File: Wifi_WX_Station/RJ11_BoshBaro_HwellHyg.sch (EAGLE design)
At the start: 8 parts, among them U1 HIH_6130

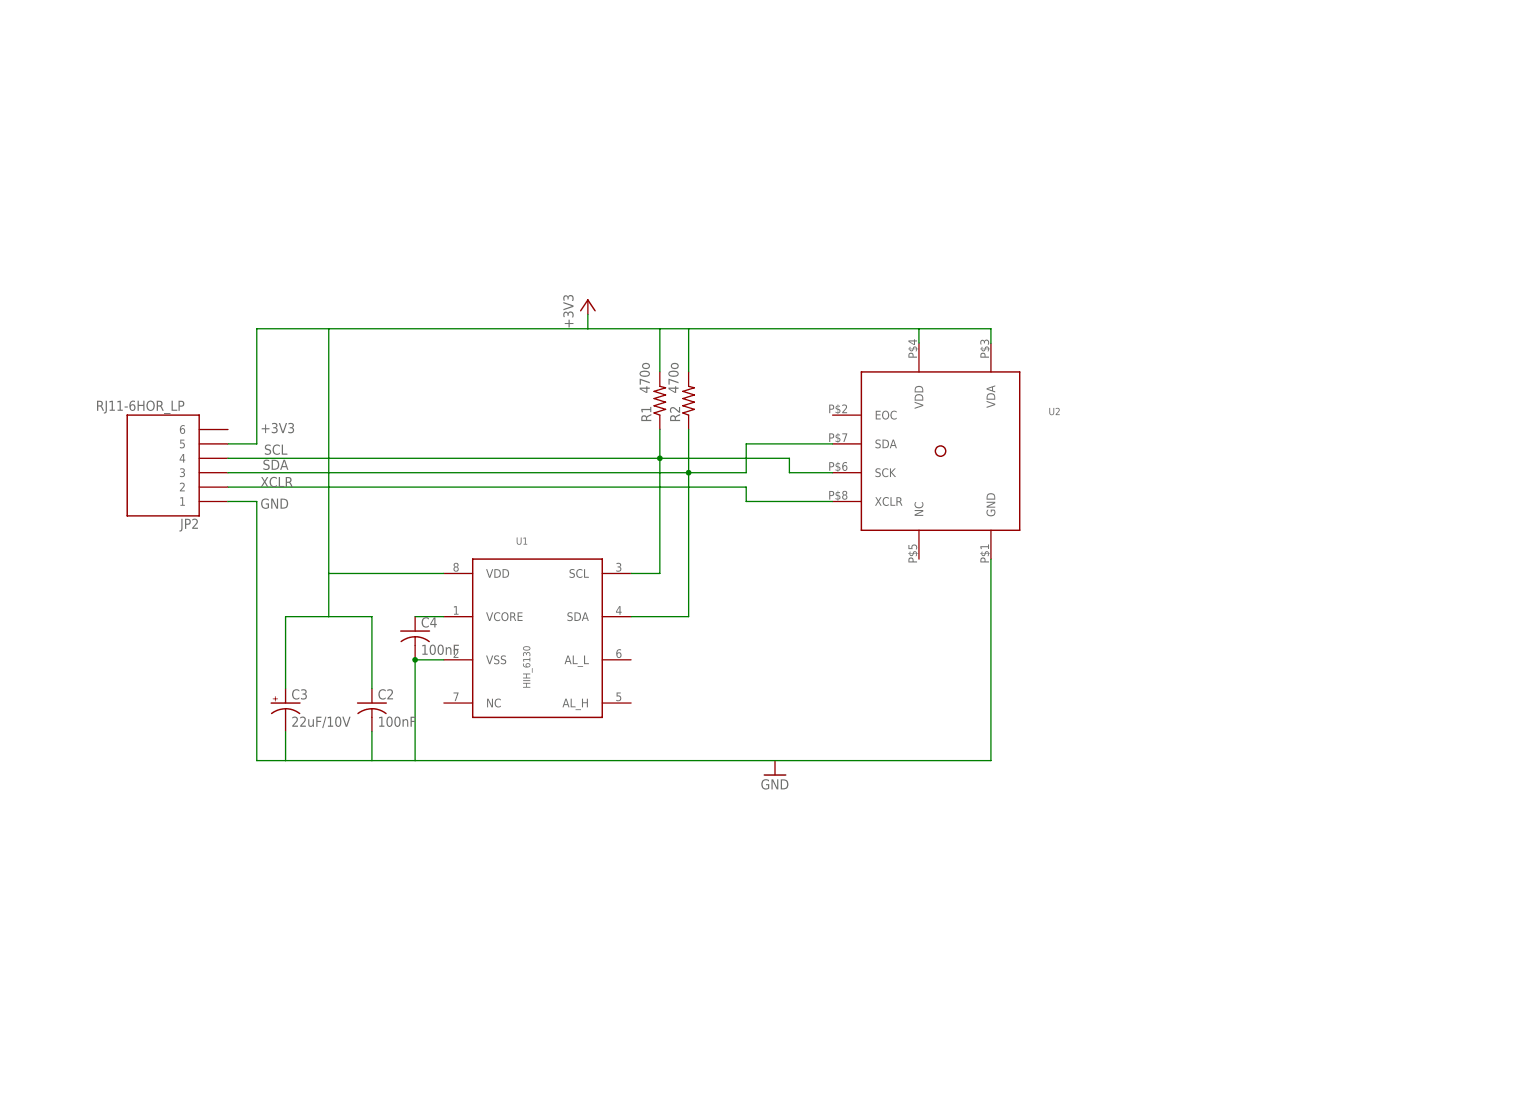
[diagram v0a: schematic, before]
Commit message: added SILabs Hygrometer board Added frames to the schematics
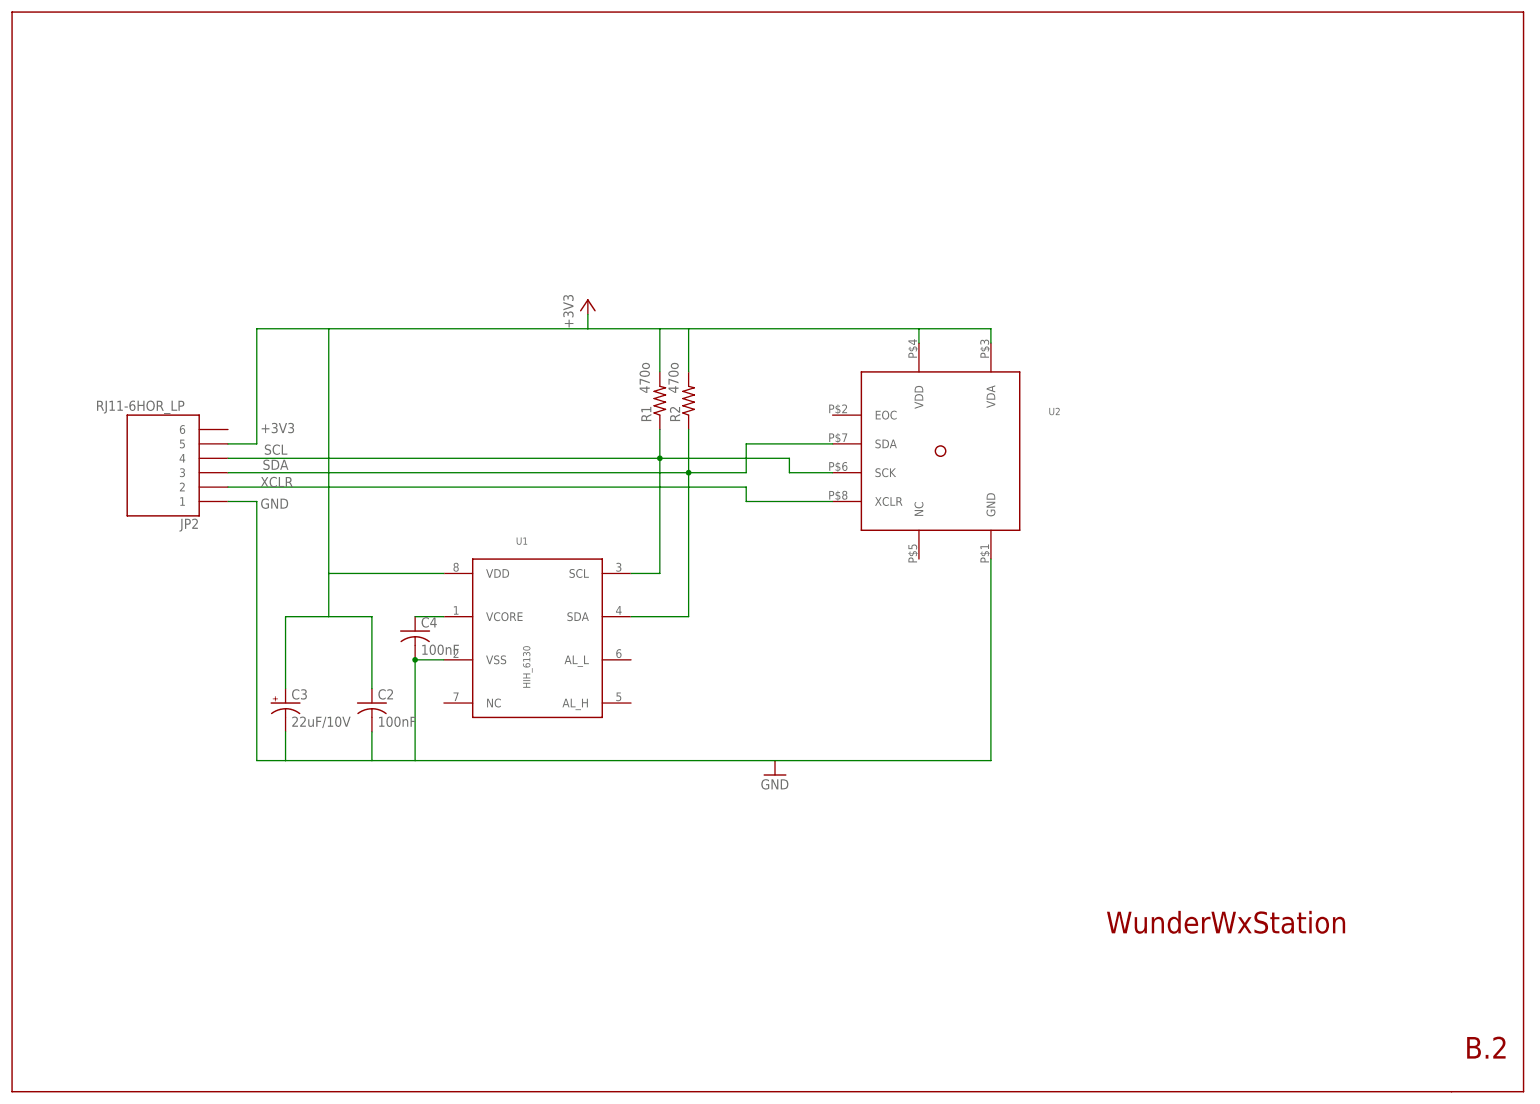
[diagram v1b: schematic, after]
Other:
- note added: "B.2"
- note added: "WunderWxStation"
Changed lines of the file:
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@@
 <part name="U2" library="1AA_Stofer" deviceset="BMP085" device=""/>
 <part name="JP2" library="wifi_WX" deviceset="RJ11-6" device="HOR_LP"/>
+<part name="U$1" library="1AA_Stofer" deviceset="8.5X11" device=""/>
 </parts>
 <sheets>
 <sheet>
 <plain>
+<text x="157.48" y="-30.48" size="3.81" layer="94" ratio="20">WunderWxStation</text>
+<text x="220.726" y="-52.578" size="3.81" layer="94" ratio="20">B.2</text>
 </plain>
 <instances>
@@
 <instance part="U2" gate="G$1" x="121.92" y="48.26"/>
 <instance part="JP2" gate="G$1" x="-7.62" y="55.88" rot="R180"/>
+<instance part="U$1" gate="G$1" x="-35.56" y="-58.42"/>
+<instance part="U$1" gate="G$2" x="129.54" y="-58.42"/>
 </instances>
 <busses>
